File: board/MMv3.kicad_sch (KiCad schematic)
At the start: 26 parts, among them J1 9V, J2 DRV8833_L, J3 left_mot, J4 right_mot, J5 DRV8833_R, Q1 DMG2301L, SW1 PWR, SW2 but, U1 DS28E05R+T, U2 LD1117S50TR_SOT223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

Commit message: Added 3D .step model of Pi Pico and whatever other settings and changes I forgot
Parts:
- U3: footprint extraparts:RPi_Pico -> RASPBERRY_PI_PICO:RASPBERRY_PI_PICO

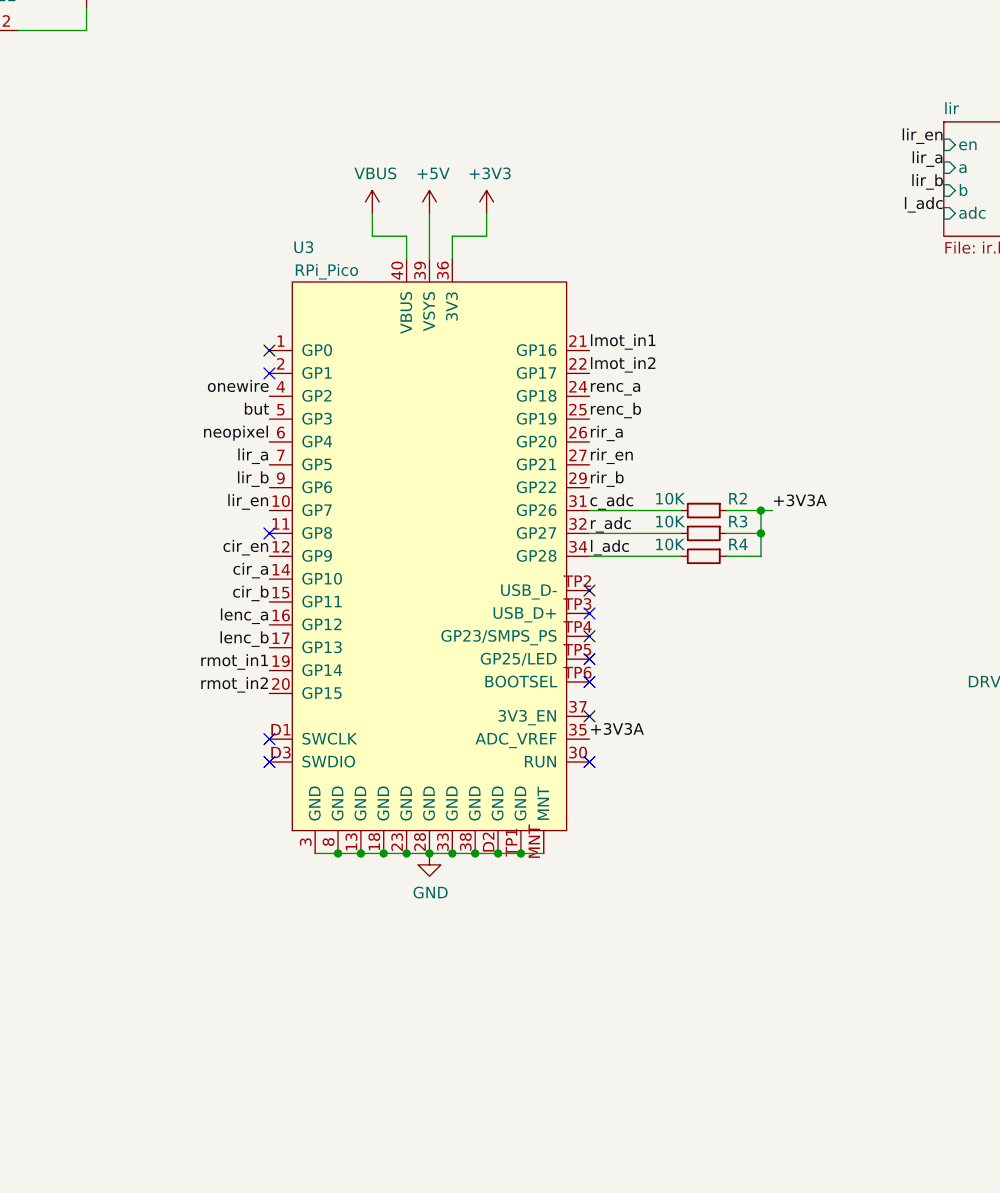
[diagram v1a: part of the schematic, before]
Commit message: Finished silkscreen and moving components
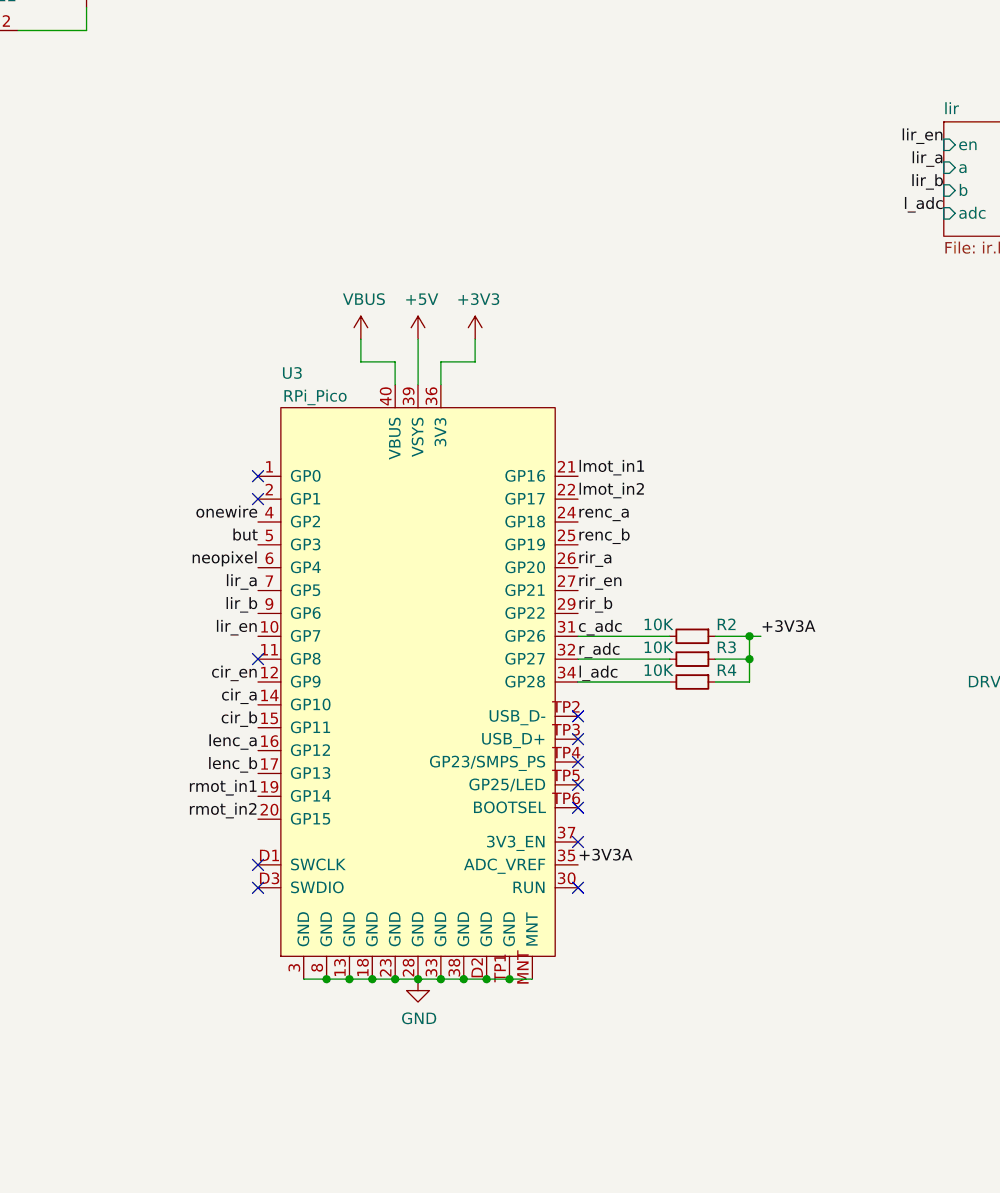
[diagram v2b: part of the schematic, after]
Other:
- moved on the sheet: R2, R3, R4, U3

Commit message: Beginning 9V Battery LED indicator schematic circuit
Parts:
- added D14: LED, symbol Device:LED
- added D15: D_Zener, symbol Device:D_Zener
- added JP1: SolderJumper_2_Open, symbol Jumper:SolderJumper_2_Open
- added R11: R, symbol Device:R
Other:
- note added: "9V Battery Level LED Indicator"

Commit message: first time running through instantDFM
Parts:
- removed D14: LED, symbol Device:LED
- removed D15: D_Zener, symbol Device:D_Zener
- removed JP1: SolderJumper_2_Open, symbol Jumper:SolderJumper_2_Open
- removed R1: 1k, Resistor_SMD:R_0805_2012Metric, symbol Device:R_Small
- removed R11: R, symbol Device:R
- removed U1: DS28E05R+T, Package_TO_SOT_SMD:SOT-23, symbol extraparts:DS28E05R+T
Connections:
- net onewire: no longer names the net of U3.4 (GP2)
- no-connect marks 17 -> 18
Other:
- note removed: "9V Battery Level LED Indicator"
- note removed: "Fun Extras"

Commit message: finished mmv3_5 now bought
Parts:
- SW2: footprint Button_Switch_SMD:SW_SPST_PTS810 -> 1825966_1 (1):SWDIP2_256X170P100
- U3: footprint RASPBERRY_PI_PICO:RASPBERRY_PI_PICO -> extraparts:RPi_Pico_SMD
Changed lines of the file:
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@@
 			)
 		)
-		(property "Footprint" "RASPBERRY_PI_PICO:RASPBERRY_PI_PICO"
+		(property "Footprint" "extraparts:RPi_Pico_SMD"
 			(at 135.89 78.74 0)
 			(effects
@@
 			)
 		)
-		(property "Footprint" "Button_Switch_SMD:SW_SPST_PTS810"
+		(property "Footprint" "1825966_1 (1):SWDIP2_256X170P100"
 			(at 81.28 87.63 0)
 			(effects
